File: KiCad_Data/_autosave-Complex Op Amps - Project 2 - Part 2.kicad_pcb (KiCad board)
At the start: 2 copper layers, 184.2 x 82.1 mm, 121 parts, among them P1 Potentiometer P/N: 3590P-2-**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, P2 Potentiometer P/N: 3590P-2-**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, SW1 SPST Switch, P/N: GT12MABE, SW2 SPST Switch, P/N: GT12MABE, SW3 SPST Switch, P/N: GT12MABE, SW4 SPST Switch, P/N: GT12MABE, SW5 SPST Switch, P/N: GT12MABE, T1 Transistor P/N: 2N3906, T2 Transistor P/N: 2N3906, T3 Transistor P/N: 2N3906, T4 Transistor P/N: 2N3906

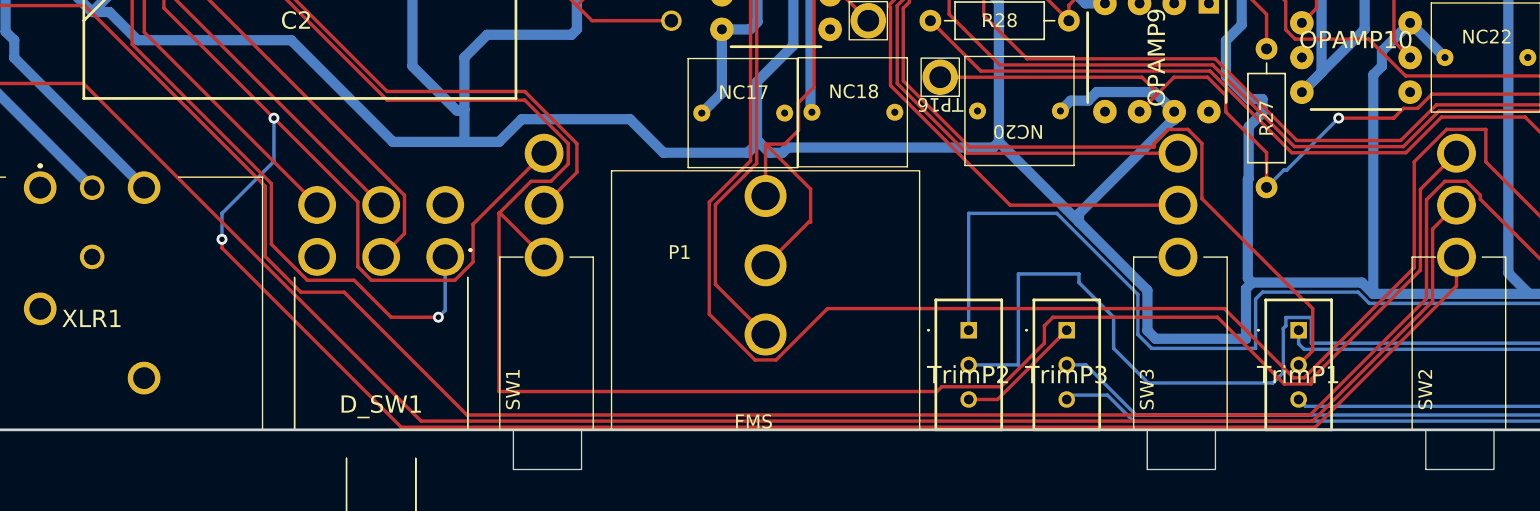
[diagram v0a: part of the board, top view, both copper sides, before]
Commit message: Updated files
Contain Kicad files which include the required capacitors on each op-amp, and additionally electrolytic capacitors were added
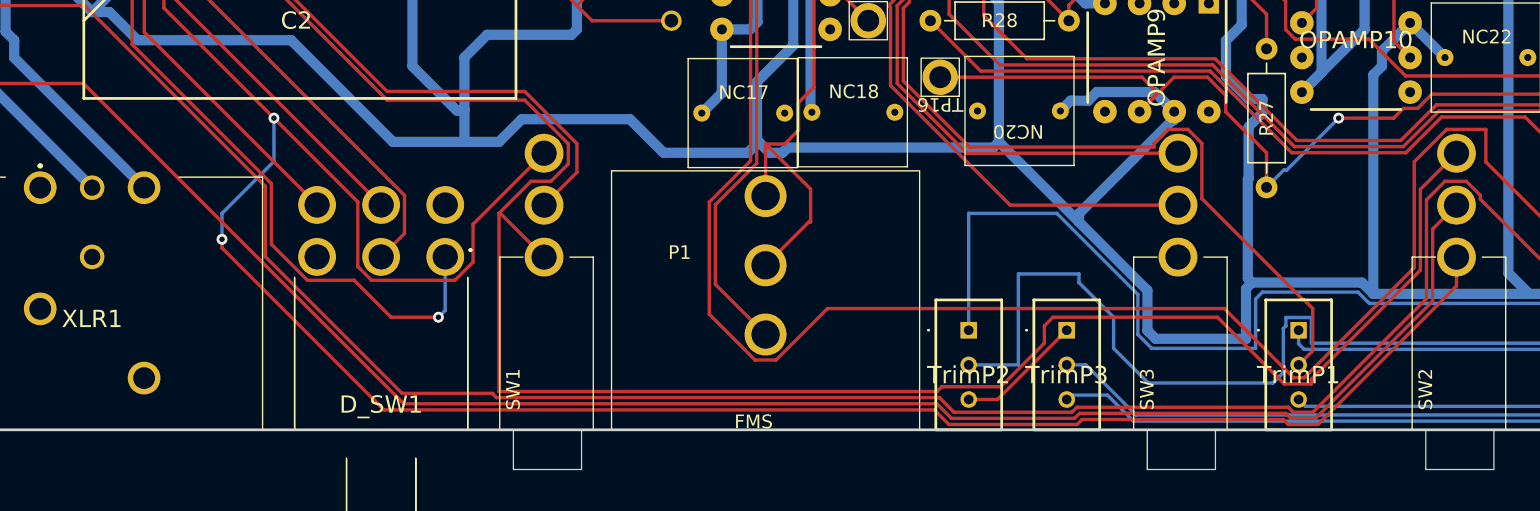
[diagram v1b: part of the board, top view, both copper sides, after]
